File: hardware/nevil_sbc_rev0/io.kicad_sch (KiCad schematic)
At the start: 29 parts, among them J301 Enable Pico 3.3V, J302 Expansion Port, J303 VIA0PB, J304 VGA Connector, J305 VIA1PA, J306 VIA1PB, J307 Keyboard, U301 74HC245, U302 Pico, U303 74HC245

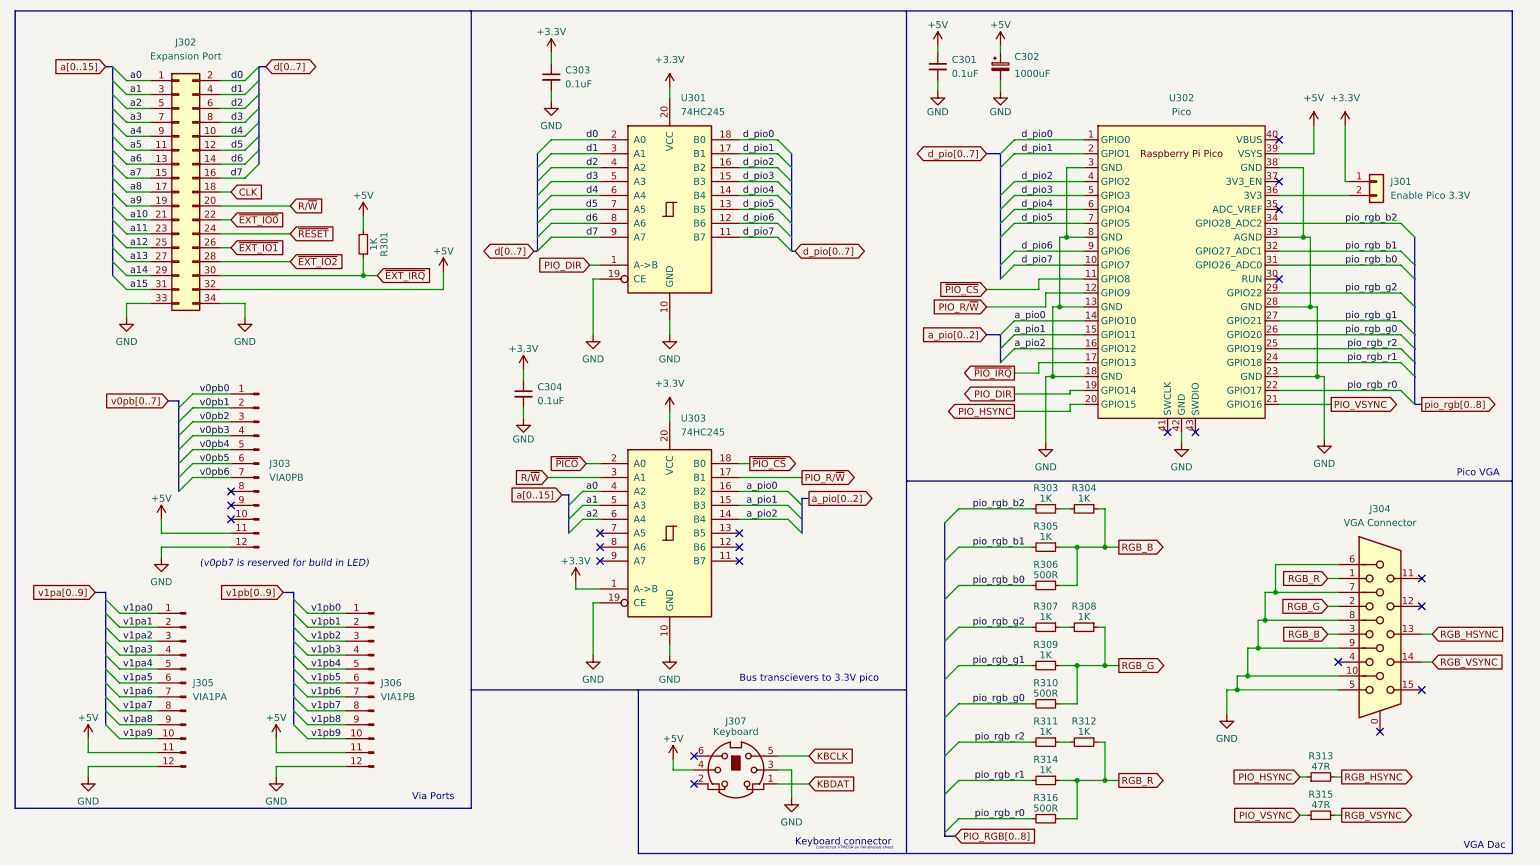
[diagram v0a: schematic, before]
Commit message: Add pcb files and small clk change for pico
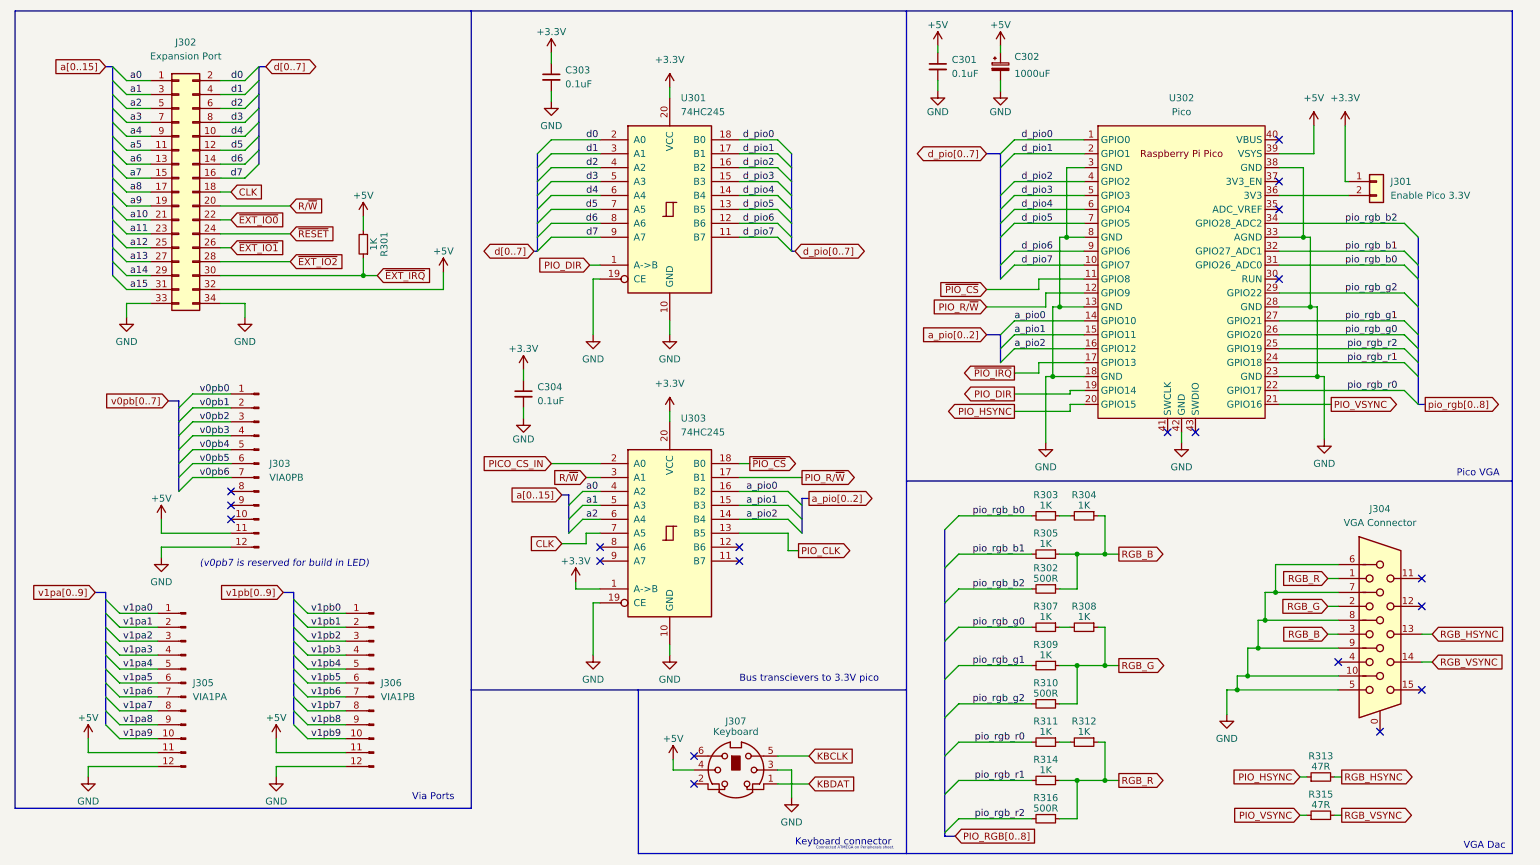
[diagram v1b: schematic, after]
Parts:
- removed R306: 500R, Resistor_THT:R_Axial_DIN0204_L3.6mm_D1.6mm_P7.62mm_Horizontal, symbol Device:R_Small
- added R302: 500R, Resistor_THT:R_Axial_DIN0204_L3.6mm_D1.6mm_P7.62mm_Horizontal, symbol Device:R_Small
- U302: footprint RPi_Pico:RPi_Pico_SMD_TH -> RPPico:RPi_Pico_SMD_TH
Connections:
- net CLK: now also U303.7 (A5)
- net RGB_B: now also R302.1
- net pio_rgb_b0: now also R303.2
- net pio_rgb_b2: now also R302.2; no longer R303.2
- net pio_rgb_g0: now also R307.2; no longer R310.2
- net pio_rgb_g2: now also R310.2; no longer R307.2
- net pio_rgb_r0: now also R311.2; no longer R316.2
- net pio_rgb_r2: now also R316.2; no longer R311.2
- net PIO_CLK: now reaches U303.13 (B5)
- net ~{PICO} renamed PICO_CS_IN
- no-connect marks 22 -> 20
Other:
- moved on the sheet: R303, R304, R305

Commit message: Working on pcb
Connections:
- net pio_rgb_b0: now also R311.2; no longer R303.2
- net pio_rgb_b1: now also R314.2; no longer R305.2
- net pio_rgb_b2: now also R316.2; no longer R302.2
- net pio_rgb_r0: now also R303.2; no longer R311.2
- net pio_rgb_r1: now also R305.2; no longer R314.2
- net pio_rgb_r2: now also R302.2; no longer R316.2
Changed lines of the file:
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@@
     (effects (font (size 1.27 1.27)) (justify left bottom))
   )
-  (label "pio_rgb_r1" (at 196.215 152.4 180)
+  (label "pio_rgb_b1" (at 196.215 152.4 180)
     (effects (font (size 1.27 1.27)) (justify right bottom))
   )
@@
     (effects (font (size 1.27 1.27)) (justify left bottom))
   )
-  (label "pio_rgb_b1" (at 196.215 111.125 180)
-    (effects (font (size 1.27 1.27)) (justify right bottom))
-  )
-  (label "pio_rgb_r0" (at 196.215 145.415 180)
+  (label "pio_rgb_r1" (at 196.215 111.125 180)
+    (effects (font (size 1.27 1.27)) (justify right bottom))
+  )
+  (label "pio_rgb_b0" (at 196.215 145.415 180)
     (effects (font (size 1.27 1.27)) (justify right bottom))
   )
@@
     (effects (font (size 1.27 1.27)) (justify left bottom))
   )
-  (label "pio_rgb_b2" (at 196.215 117.475 180)
+  (label "pio_rgb_r2" (at 196.215 117.475 180)
     (effects (font (size 1.27 1.27)) (justify right bottom))
   )
@@
     (effects (font (size 1.27 1.27)) (justify left bottom))
   )
-  (label "pio_rgb_r2" (at 196.215 159.385 180)
+  (label "pio_rgb_b2" (at 196.215 159.385 180)
     (effects (font (size 1.27 1.27)) (justify right bottom))
   )
@@
     (effects (font (size 1.27 1.27)) (justify left bottom))
   )
-  (label "pio_rgb_b0" (at 196.215 104.14 180)
-    (effects (font (size 1.27 1.27)) (justify right bottom))
-  )
+  (label "pio_rgb_r0" (at 196.215 104.14 180)
+    (effects (font (size 1.27 1.27)) (justify right bottom))
+  )

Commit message: working on vga code
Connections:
- net CLK: no longer U303.7 (A5)
- net GND: now also J304.0
- net PIO_CLK: no longer names the net of U303.13 (B5)
- net a15 renamed ~{RAM}
- net ~{EXT_IRQ} renamed ~{EXT_IO_IRQ}
- no-connect marks 20 -> 21
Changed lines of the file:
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@@
   (junction (at 205.74 152.4) (diameter 0) (color 0 0 0 0)
   )
-  (no_connect (at 260.985 143.51))
   (no_connect (at 253.365 130.81))
   (no_connect (at 135.89 147.955))
@@
   (no_connect (at 227.33 88.9))
   (no_connect (at 222.25 88.9))
+  (no_connect (at 118.745 107.315))
+  (no_connect (at 144.145 107.315))
   (bus_entry (at 184.15 117.475) (size -2.54 2.54)
     (stroke (width 0) (type default) (color 0 0 0 0))
@@
     (stroke (width 0) (type default) (color 0 0 0 0))
   )
-  (bus_entry (at 32.385 62.865) (size -2.54 -2.54)
-    (stroke (width 0) (type default) (color 0 0 0 0))
-  )
   (bus_entry (at 265.43 68.58) (size 2.54 2.54)
     (stroke (width 0) (type default) (color 0 0 0 0))
@@
     (stroke (width 0) (type default) (color 0 0 0 0))
   )
-  (wire (pts (xy 116.205 107.315) (xy 116.205 109.22))
-    (stroke (width 0) (type default) (color 0 0 0 0))
-  )
   (wire (pts (xy 184.15 138.43) (xy 197.485 138.43))
     (stroke (width 0) (type default) (color 0 0 0 0))
@@
     (stroke (width 0) (type default) (color 0 0 0 0))
   )
-  (bus (pts (xy 29.845 57.785) (xy 29.845 60.325))
-    (stroke (width 0) (type default) (color 0 0 0 0))
-  )
   (bus (pts (xy 62.865 137.16) (xy 62.865 139.7))
     (stroke (width 0) (type default) (color 0 0 0 0))
@@
     (stroke (width 0) (type default) (color 0 0 0 0))
   )
-  (wire (pts (xy 116.205 109.22) (xy 111.76 109.22))
-    (stroke (width 0) (type default) (color 0 0 0 0))
-  )
   (wire (pts (xy 131.445 127.635) (xy 131.445 129.54))
     (stroke (width 0) (type default) (color 0 0 0 0))
@@
     (stroke (width 0) (type default) (color 0 0 0 0))
   )
+  (wire (pts (xy 260.985 145.415) (xy 260.985 143.51))
+    (stroke (width 0) (type default) (color 0 0 0 0))
+  )
   (wire (pts (xy 115.57 104.775) (xy 118.745 104.775))
     (stroke (width 0) (type default) (color 0 0 0 0))
@@
     (stroke (width 0) (type default) (color 0 0 0 0))
   )
-  (wire (pts (xy 118.745 107.315) (xy 116.205 107.315))
-    (stroke (width 0) (type default) (color 0 0 0 0))
-  )
   (bus (pts (xy 181.61 147.955) (xy 181.61 154.94))
     (stroke (width 0) (type default) (color 0 0 0 0))
@@
     (stroke (width 0) (type default) (color 0 0 0 0))
   )
-  (wire (pts (xy 154.94 110.49) (xy 153.035 110.49))
-    (stroke (width 0) (type default) (color 0 0 0 0))
-  )
   (wire (pts (xy 59.69 147.32) (xy 59.69 144.78))
     (stroke (width 0) (type default) (color 0 0 0 0))
@@
     (stroke (width 0) (type default) (color 0 0 0 0))
   )
-  (wire (pts (xy 153.035 110.49) (xy 153.035 107.315))
-    (stroke (width 0) (type default) (color 0 0 0 0))
-  )
   (wire (pts (xy 201.295 78.74) (xy 207.01 78.74))
     (stroke (width 0) (type default) (color 0 0 0 0))
@@
   )
   (wire (pts (xy 242.57 73.66) (xy 265.43 73.66))
-    (stroke (width 0) (type default) (color 0 0 0 0))
-  )
-  (wire (pts (xy 153.035 107.315) (xy 144.145 107.315))
     (stroke (width 0) (type default) (color 0 0 0 0))
   )
@@
   )
   (label "d_pio2" (at 195.58 43.18 0)
-    (effects (font (size 1.27 1.27)) (justify left bottom))
-  )
-  (label "a15" (at 33.02 62.865 0)
     (effects (font (size 1.27 1.27)) (justify left bottom))
   )
@@
     )
   )
-  (global_label "CLK" (shape input) (at 111.76 109.22 180) (fields_autoplaced)
-    (effects (font (size 1.27 1.27)) (justify right))
-    (property "Intersheet References" "${INTERSHEET_REFS}" (id 0) (at 105.7788 109.1406 0)
-      (effects (font (size 1.27 1.27)) (justify right) hide)
-    )
-  )
   (global_label "PIO_DIR" (shape output) (at 194.31 81.915 180) (fields_autoplaced)
     (effects (font (size 1.27 1.27)) (justify right))
@@
     )
   )
-  (global_label "PIO_CLK" (shape output) (at 154.94 110.49 0) (fields_autoplaced)
-    (effects (font (size 1.27 1.27)) (justify left))
-    (property "Intersheet References" "${INTERSHEET_REFS}" (id 0) (at 165.0941 110.4106 0)
-      (effects (font (size 1.27 1.27)) (justify left) hide)
-    )
-  )
   (global_label "RGB_HSYNC" (shape input) (at 270.51 125.73 0) (fields_autoplaced)
     (effects (font (size 1.27 1.27)) (justify left))
@@
     )
   )
+  (global_label "~{RAM}" (shape input) (at 32.385 62.865 180) (fields_autoplaced)
+    (effects (font (size 1.27 1.27)) (justify right))
+    (property "Intersheet References" "${INTERSHEET_REFS}" (id 0) (at 26.1619 62.7856 0)
+      (effects (font (size 1.27 1.27)) (justify right) hide)
+    )
+  )
   (global_label "~{PIO_IRQ}" (shape output) (at 194.31 78.105 180) (fields_autoplaced)
     (effects (font (size 1.27 1.27)) (justify right))
@@
     )
   )
-  (global_label "~{EXT_IRQ}" (shape input) (at 78.105 60.325 0) (fields_autoplaced)
+  (global_label "~{EXT_IO_IRQ}" (shape input) (at 78.105 60.325 0) (fields_autoplaced)
     (effects (font (size 1.27 1.27)) (justify left))
-    (property "Intersheet References" "${INTERSHEET_REFS}" (id 0) (at 88.0171 60.2456 0)
+    (property "Intersheet References" "${INTERSHEET_REFS}" (id 0) (at 90.92 60.2456 0)
       (effects (font (size 1.27 1.27)) (justify left) hide)
     )
@@
     (pin "9")
   )
+  (symbol (lib_id "power:GND") (at 260.985 145.415 0) (unit 1)
+    (in_bom yes) (on_board yes) (fields_autoplaced)
+    (property "Reference" "#PWR0199" (id 0) (at 260.985 151.765 0)
+      (effects (font (size 1.27 1.27)) hide)
+    )
+    (property "Value" "GND" (id 1) (at 260.985 149.86 0))
+    (property "Footprint" "" (id 2) (at 260.985 145.415 0)
+      (effects (font (size 1.27 1.27)) hide)
+    )
+    (property "Datasheet" "" (id 3) (at 260.985 145.415 0)
+      (effects (font (size 1.27 1.27)) hide)
+    )
+    (pin "1")
+  )
   (symbol (lib_id "Connector_Generic:Conn_02x17_Odd_Even") (at 41.91 45.085 0) (unit 1)
